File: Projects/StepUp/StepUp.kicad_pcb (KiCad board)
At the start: 2 copper layers, 80 parts, among them J1 Conn_01x02, J4 Conn_01x02, J5 Conn_01x02, J7 Conn_01x02, J8 USB_C_Receptacle_USB2.0_16P, Q1 BSS83P, Q2 BSS83P, SW1 SW_Push, SW2 SW_Push, U1 W25Q128JVS, U2 RP2040, U3 TMC2300-LA, U4 USBLC6-2SC6, U5 MCP73832T-2ACI_OT, U6 NCP1117-3.3_SOT223, U7 MIC2253, U8 COM-09032, Y1 ABM8-272-T3

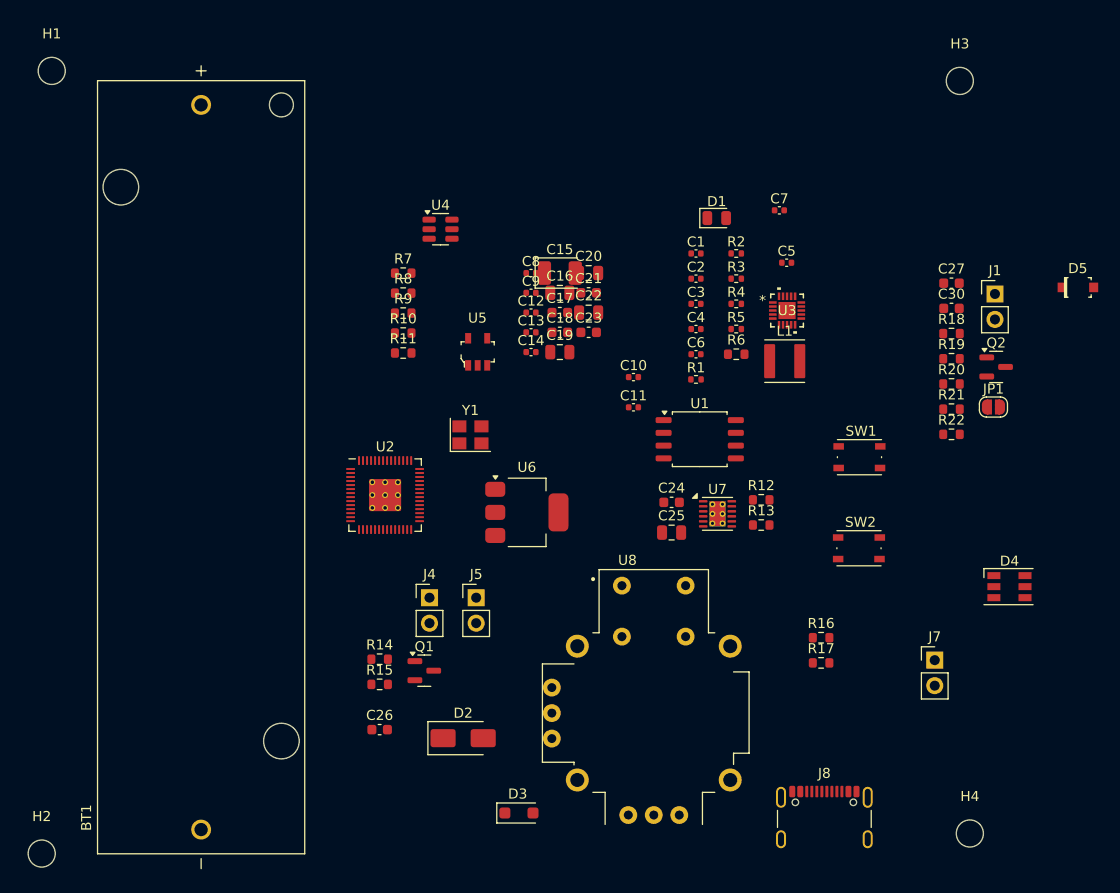
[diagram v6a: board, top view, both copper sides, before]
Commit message: feat(stepup): Schematic + PCB updates
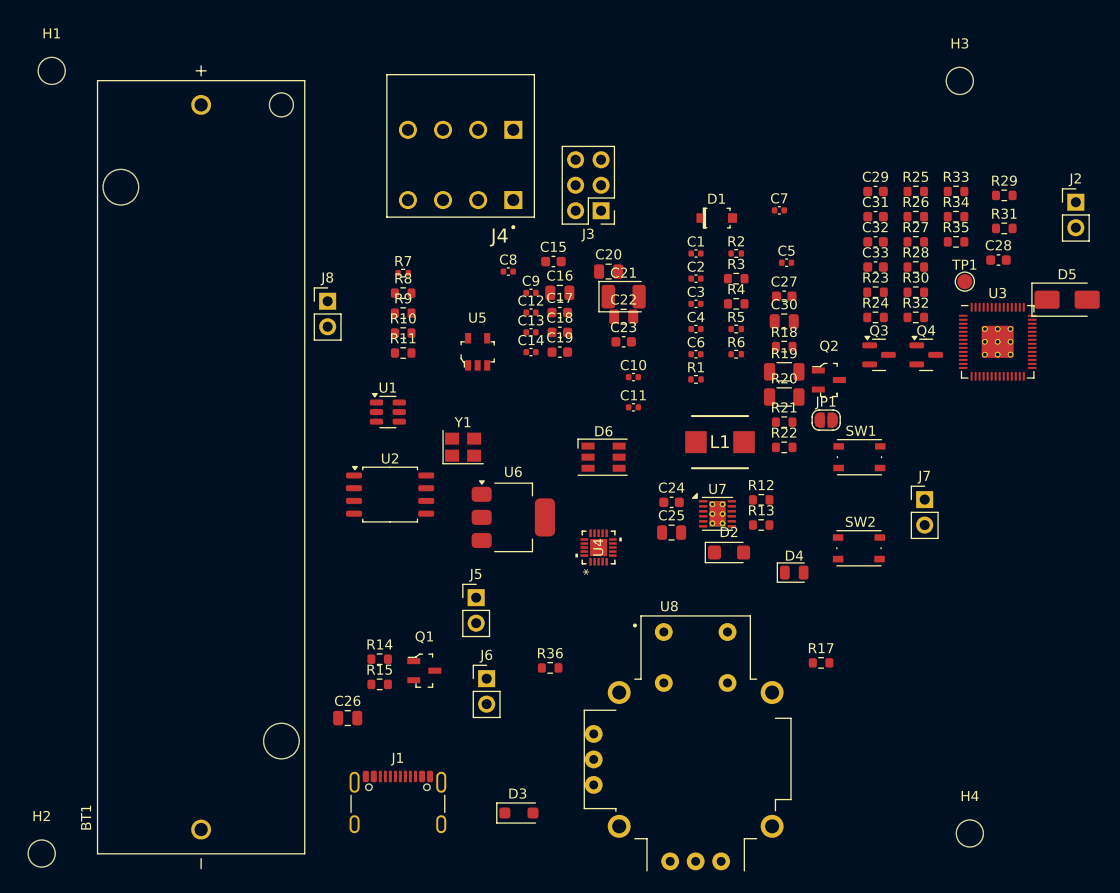
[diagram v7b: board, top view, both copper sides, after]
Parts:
- removed R16: 5.1kR, Resistor_SMD:R_0603_1608Metric
- added C28: 0.01uF, Capacitor_SMD:C_0603_1608Metric, F.Cu at (183.9, 84.4)
- added C29: 100pF, Capacitor_SMD:C_0603_1608Metric, F.Cu at (171.6, 77.5)
- added C31: 0.1uF, Capacitor_SMD:C_0603_1608Metric, F.Cu at (171.6, 80.0)
- added C32: 0.1uF, Capacitor_SMD:C_0603_1608Metric, F.Cu at (171.6, 82.5)
- added C33: 0.1uF, Capacitor_SMD:C_0603_1608Metric, F.Cu at (171.6, 85.1)
- added D6: CLX6F-FKC, LED_SMD:LED_RGB_PLCC-6, F.Cu at (144.5, 104.0)
- added J2: Conn_01x02, Connector_PinHeader_2.54mm:PinHeader_1x02_P2.54mm_Vertical, F.Cu at (191.6, 78.6)
- added J3: Conn_02x03_Counter_Clockwise, Connector_PinHeader_2.54mm:PinHeader_2x03_P2.54mm_Vertical, F.Cu at (144.2, 79.4)
- added J6: Conn_01x02, Connector_PinHeader_2.54mm:PinHeader_1x02_P2.54mm_Vertical, F.Cu at (132.8, 126.1)
- added Q3: BSS83P, Package_TO_SOT_SMD:SOT-23, F.Cu at (171.9, 93.8)
- added Q4: BSS83P, Package_TO_SOT_SMD:SOT-23, F.Cu at (176.6, 93.8)
- added R23: 510R, Resistor_SMD:R_0603_1608Metric, F.Cu at (171.6, 87.6)
- added R24: Rled, Resistor_SMD:R_0603_1608Metric, F.Cu at (171.6, 90.1)
- added R25: 100kR, Resistor_SMD:R_0603_1608Metric, F.Cu at (175.6, 77.5)
- added R26: 620R, Resistor_SMD:R_0603_1608Metric, F.Cu at (175.6, 80.0)
- added R27: 100R, Resistor_SMD:R_0603_1608Metric, F.Cu at (175.6, 82.5)
- added R28: 71.5kR, Resistor_SMD:R_0603_1608Metric, F.Cu at (175.6, 85.1)
- added R29: 10kR, Resistor_SMD:R_0603_1608Metric, F.Cu at (184.4, 77.9)
- added R30: 100kR, Resistor_SMD:R_0603_1608Metric, F.Cu at (175.6, 87.6)
- added R31: 9.09kR, Resistor_SMD:R_0603_1608Metric, F.Cu at (184.4, 81.2)
- added R32: 10kR, Resistor_SMD:R_0603_1608Metric, F.Cu at (175.6, 90.1)
- added R33: 100kR, Resistor_SMD:R_0603_1608Metric, F.Cu at (179.6, 77.5)
- added R34: 100kR, Resistor_SMD:R_0603_1608Metric, F.Cu at (179.6, 80.0)
- added R35: 100kR, Resistor_SMD:R_0603_1608Metric, F.Cu at (179.6, 82.5)
- added R36: 100kR, Resistor_SMD:R_0603_1608Metric, F.Cu at (139.2, 125.0)
- added TP1: TestPoint, TestPoint:TestPoint_Pad_D1.5mm, F.Cu at (180.5, 86.5)
- C15: value 100uF -> 100nF; footprint Capacitor_Tantalum_SMD:CP_EIA-3528-12_Kemet-T -> Capacitor_SMD:C_0603_1608Metric
- C16: value 4.7u -> 10uF
- C17: value 2.2uF -> 100nF
- C18: value 0.01uF -> 100nF
- C19: value 4.7u -> 100nF; footprint Capacitor_SMD:C_0805_2012Metric -> Capacitor_SMD:C_0603_1608Metric
- C20: value 10u -> 10uF
- C21: value 0.1uF -> 100uF; footprint Capacitor_SMD:C_0603_1608Metric -> Capacitor_Tantalum_SMD:CP_EIA-3528-12_Kemet-T
- C22: value 10u -> 4.7u
- C23: value 0.01uF -> 2.2uF
- C24: value 100pF -> 0.01uF
- C25: value 22uF -> 4.7u
- C26: value 0.1uF -> 10uF; footprint Capacitor_SMD:C_0603_1608Metric -> Capacitor_SMD:C_0805_2012Metric
- C30: value 0.1uF -> 22uF; footprint Capacitor_SMD:C_0603_1608Metric -> Capacitor_SMD:C_0805_2012Metric
- D1: value LED -> 1N4148W-TP; footprint LED_SMD:LED_0805_2012Metric -> digikey-footprints:SOD-123
- D2: value SK54A-LTP -> SMF12A; footprint Diode_SMD:D_SMA -> Diode_SMD:D_SMF
- D4: value CLX6F-FKC -> LED; footprint LED_SMD:LED_RGB_PLCC-6 -> LED_SMD:LED_0805_2012Metric
- D5: value 1N4148W-TP -> SK54A-LTP; footprint digikey-footprints:SOD-123 -> Diode_SMD:D_SMA
- J1: value Conn_01x02 -> USB_C_Receptacle_USB2.0_16P; footprint Connector_PinHeader_2.54mm:PinHeader_1x02_P2.54mm_Vertical -> Connector_USB:USB_C_Receptacle_GCT_USB4105-xx-A_16P_TopMnt_Horizontal
- J4: value Conn_01x02 -> TBLH10-350-04BK; footprint Connector_PinHeader_2.54mm:PinHeader_1x02_P2.54mm_Vertical -> Snapeda:CUI_TBLH10-350-04BK
- J8: value USB_C_Receptacle_USB2.0_16P -> Conn_01x02; footprint Connector_USB:USB_C_Receptacle_GCT_USB4105-xx-A_16P_TopMnt_Horizontal -> Connector_PinHeader_2.54mm:PinHeader_1x02_P2.54mm_Vertical
- L1: value 2.2 uH -> ASPI-0530HI-2R2M-T2; footprint Inductor_SMD:L_Abracon_ASPI-4030S -> Samacsys:INDPM5652X300N
- Q1: value BSS83P -> BSS84; footprint Package_TO_SOT_SMD:SOT-23 -> digikey-footprints:SOT-23-3
- Q2: value BSS83P -> 2N7002; footprint Package_TO_SOT_SMD:SOT-23 -> digikey-footprints:SOT-23-3
- R10: value 71.5kR -> 10kR
- R12: value 9.09kR -> 10kR
- R14: value 100R -> 10kR
- R15, R8: value 100kR -> 10kR
- R17: value 5.1kR -> 1kR
- R18: value 10kR -> 100kR
- R19, R20: value 100kR -> 150mR; footprint Resistor_SMD:R_0603_1608Metric -> Resistor_SMD:R_1206_3216Metric
- R22: value 100kR -> 100R
- R3: value 1k -> 5.1kR; footprint Resistor_SMD:R_0402_1005Metric -> Resistor_SMD:R_0603_1608Metric
- R4: value 27 -> 5.1kR; footprint Resistor_SMD:R_0402_1005Metric -> Resistor_SMD:R_0603_1608Metric
- R5: value 27 -> 1k
- R6: value RProg -> 27; footprint Resistor_SMD:R_0603_1608Metric -> Resistor_SMD:R_0402_1005Metric
- R7: value Rled -> 27; footprint Resistor_SMD:R_0603_1608Metric -> Resistor_SMD:R_0402_1005Metric
- R9: value 620R -> 10kR
- U1: value W25Q128JVS -> USBLC6-2SC6; footprint Package_SO:SOIC-8_5.23x5.23mm_P1.27mm -> Package_TO_SOT_SMD:SOT-23-6
- U2: value RP2040 -> W25Q128JVS; footprint RP2040_minimal_r2:RP2040-QFN-56 -> Package_SO:SOIC-8_5.23x5.23mm_P1.27mm
- U3: value TMC2300-LA -> RP2040; footprint Ultra_librarian_footprints:QFN20_3x3_TRI -> RP2040_minimal_r2:RP2040-QFN-56
- U4: value USBLC6-2SC6 -> TMC2300-LA; footprint Package_TO_SOT_SMD:SOT-23-6 -> Ultra_librarian_footprints:QFN20_3x3_TRI
- moved J1 78.9 mm to (124.0, 139.5)
- moved J8 72.2 mm to (117.0, 88.5)
- moved J4 40.5 mm to (135.5, 78.4), turned to 180 degrees
- moved U4 35.4 mm to (144.0, 113.0), turned to 90 degrees
- moved D2 32.3 mm to (157.0, 113.5)
- moved U1 31.2 mm to (123.0, 99.5)
- moved D4 21.5 mm to (163.5, 115.5)
- moved U3 21.2 mm to (183.8, 92.5)
- moved Q2 16.7 mm to (166.9, 96.3)
- moved R21 16.7 mm to (162.5, 100.5)
- moved C27 16.7 mm to (162.5, 88.0)
- moved C30 16.7 mm to (162.5, 90.5)
- moved JP1 16.7 mm to (166.7, 100.3)
- moved R18 16.7 mm to (162.5, 93.0)
- moved R19 16.7 mm to (162.5, 95.5)
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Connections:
- C15 pad 1: /Power/BOOST_VIN -> VMotor
- C15 pad 2: GND -> Net-(U4-VCP)
- C16 pad 1: GND -> VMotor
- C16 pad 2: V_USB -> GND
- C17 pad 1: /Power/BOOST_VIN -> VMotor
- C18 pad 1: /Power/BOOST_VIN -> /Motor Driver/VCC_IO
- C19 pad 1: Net-(J4-Pin_2) -> Net-(U4-1.8VOUT)
- C21 pad 1: Net-(U7-SS) -> /Power/BOOST_VIN
- C22 pad 1: +3V3 -> GND
- C22 pad 2: GND -> V_USB
- C23 pad 1: Net-(C23-Pad1) -> /Power/BOOST_VIN
- C24 pad 1: /Power/BOOST_VOUT -> /Power/BOOST_VIN
- C24 pad 2: Net-(U7-FB) -> GND
- C25 pad 1: /Power/BOOST_VOUT -> Net-(J7-Pin_2)
- C27 pad 1: GND -> Net-(U7-SS)
- C27 pad 2: Vbat_monitor -> GND
- C30 pad 1: GND -> /Power/BOOST_VOUT
- C30 pad 2: VUSB_monitor -> GND
- D2 pad 1: /Power/BOOST_VOUT -> VMotor
- D2 pad 2: Net-(D2-A) -> GND
- D4 pad 1: unconnected-(D4-KB-Pad1) -> Net-(D4-K)
- D4 pad 2: unconnected-(D4-KG-Pad2) -> V_USB
- J5 pad 2: Net-(J5-Pin_2) -> Net-(D3-A)
- J7 pad 2: /Power/BOOST_VIN -> Net-(J7-Pin_2)
- L1 pad 2: Net-(D2-A) -> Net-(D5-A)
- Q1 pad 2: /Power/BOOST_ENABLE -> +3V3
- Q1 pad 3: /Power/MCU_BOOST_EN -> /Motor Driver/VCC_IO
- Q2 pad 1: Net-(D3-A) -> ~{TMC_STBDY}
- Q2 pad 2: Net-(D3-K) -> GND
- Q2 pad 3: Vbat -> Net-(Q1-G)
- R10 pad 1: Net-(U7-OVP) -> /Motor Driver/VCC_IO
- R10 pad 2: /Power/BOOST_VOUT -> GND
- R11 pad 1: GND -> TMC_EN
- R11 pad 2: Net-(U7-OVP) -> GND
- R12 pad 1: Net-(U7-FB) -> TMC_STEP
- R12 pad 2: /Power/BOOST_VOUT -> GND
- R13 pad 1: GND -> TMC_DIR
- R13 pad 2: Net-(U7-FB) -> GND
- R14 pad 1: V_USB -> /Motor Driver/VCC_IO
- R14 pad 2: Net-(Q1-G) -> /Motor Driver/TMC_MS2/AD1
- R15 pad 1: GND -> /Motor Driver/VCC_IO
- R15 pad 2: Net-(Q1-G) -> /Motor Driver/TMC_MS1/AD0
- R17 pad 1: GND -> TMC_UART_RX
- R17 pad 2: Net-(J8-CC2) -> TMC_UART_TX
- R18 pad 1: Net-(D3-A) -> TMC_UART_RX
- R19 pad 2: Vbat_monitor -> Net-(U4-BRA)
- R20 pad 1: Vbat_monitor -> GND
- R20 pad 2: Vbat -> Net-(U4-BRB)
- R21 pad 1: VUSB_monitor -> GND
- R21 pad 2: V_USB -> Net-(D3-A)
- R22 pad 1: GND -> Net-(D3-A)
- R22 pad 2: VUSB_monitor -> Net-(Q3-G)
- R3 pad 1: /MCU/XOUT -> GND
- R3 pad 2: Net-(C2-Pad1) -> Net-(J1-CC1)
- R4 pad 1: /MCU/USB_D+ -> GND
- R4 pad 2: Net-(U2-USB_DP) -> Net-(J1-CC2)
- R5 pad 1: /MCU/USB_D- -> /MCU/XOUT
- R5 pad 2: Net-(U2-USB_DM) -> Net-(C2-Pad1)
- R6 pad 1: GND -> /MCU/USB_D+
- R6 pad 2: Net-(U5-PROG) -> Net-(U3-USB_DP)
- R7 pad 1: Net-(U5-STAT) -> /MCU/USB_D-
- R7 pad 2: Net-(D1-K) -> Net-(U3-USB_DM)
- R8 pad 1: GND -> ~{TMC_STBDY}
- R8 pad 2: /Power/BOOST_ENABLE -> GND
- R9 pad 1: Net-(U7-COMP) -> Net-(Q1-G)
- R9 pad 2: Net-(C23-Pad1) -> +3V3
- SW1 pad 2: Net-(D5-PadK) -> /MCU/RUN
- SW2 pad 2: /MCU/RUN -> Net-(D1-PadK)
- U1 pad 1: /MCU/QSPI_SS -> /MCU/USB_D-_IN
- U1 pad 2: /MCU/QSPI_SD1 -> GND
- U1 pad 3: /MCU/QSPI_SD2 -> /MCU/USB_D+_IN
- U1 pad 4: GND -> /MCU/USB_D+
- U1 pad 5: /MCU/QSPI_SD0 -> Net-(J2-Pin_2)
- U1 pad 6: /MCU/QSPI_SCLK -> /MCU/USB_D-
- U2 pad 1: +3V3 -> /MCU/QSPI_SS
- U2 pad 2: /MCU/GPIO0 -> /MCU/QSPI_SD1
- U2 pad 3: /MCU/GPIO1 -> /MCU/QSPI_SD2
- U2 pad 4: /MCU/GPIO2 -> GND
- U2 pad 5: /MCU/GPIO3 -> /MCU/QSPI_SD0
- U2 pad 6: /MCU/GPIO4 -> /MCU/QSPI_SCLK
- U2 pad 7: /MCU/GPIO5 -> /MCU/QSPI_SD3
- U2 pad 8: /MCU/GPIO6 -> +3V3
- U3 pad 1: unconnected-(U3-OA2-Pad1) -> +3V3
- U3 pad 10: unconnected-(U3-PDN_UART-Pad10) -> +3V3
- U3 pad 11: unconnected-(U3-VIO/NSTDBY-Pad11) -> /MCU/GPIO8
- U3 pad 12: unconnected-(U3-DIAG-Pad12) -> /MCU/GPIO9
- U3 pad 13: unconnected-(U3-1.8VOUT-Pad13) -> /MCU/GPIO10
- U3 pad 14: unconnected-(U3-GND-Pad14) -> /MCU/GPIO11
- U3 pad 15: unconnected-(U3-OB2-Pad15) -> /MCU/GPIO12
- U3 pad 16: unconnected-(U3-BRB-Pad16) -> /MCU/GPIO13
- U3 pad 17: unconnected-(U3-OB1-Pad17) -> TMC_EN
- U3 pad 18: unconnected-(U3-VS-Pad18) -> ~{TMC_STBDY}
- U3 pad 19: unconnected-(U3-OA1-Pad19) -> GND
- U3 pad 2: unconnected-(U3-VCP-Pad2) -> /MCU/UART_0_TX
- U3 pad 20: unconnected-(U3-BRA-Pad20) -> /MCU/XIN
- U3 pad 21: unconnected-(U3-EPAD-Pad21) -> /MCU/XOUT
- U3 pad 3: unconnected-(U3-DIR-Pad3) -> /MCU/UART_0_RX
- U3 pad 4: unconnected-(U3-STEP-Pad4) -> /MCU/GPIO2
- U3 pad 5: unconnected-(U3-MS1_AD0-Pad5) -> /MCU/GPIO3
- U3 pad 6: unconnected-(U3-MS2_AD1-Pad6) -> TMC_UART_TX
- U3 pad 7: unconnected-(U3-EN-Pad7) -> TMC_UART_RX
- U3 pad 8: unconnected-(U3-STEPPER-Pad8) -> /MCU/GPIO6
- U3 pad 9: unconnected-(U3-MODE-Pad9) -> /MCU/GPIO7
- U4 pad 1: /Power/USB_D+_IN -> /Motor Driver/OA2
- U4 pad 2: GND -> Net-(U4-VCP)
- U4 pad 3: /Power/USB_D-_IN -> TMC_DIR
- U4 pad 4: /Power/USB_D- -> TMC_STEP
- U4 pad 5: Net-(J5-Pin_2) -> /Motor Driver/TMC_MS1/AD0
- U4 pad 6: /Power/USB_D+ -> /Motor Driver/TMC_MS2/AD1
- U5 pad 3: Net-(J4-Pin_2) -> Net-(J7-Pin_2)
- U7 pad 7: Net-(D2-A) -> Net-(D5-A)
- U7 pad 8: Net-(D2-A) -> Net-(D5-A)
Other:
- copper layers 2 -> 4

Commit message: feat(schematic): Ready for layout
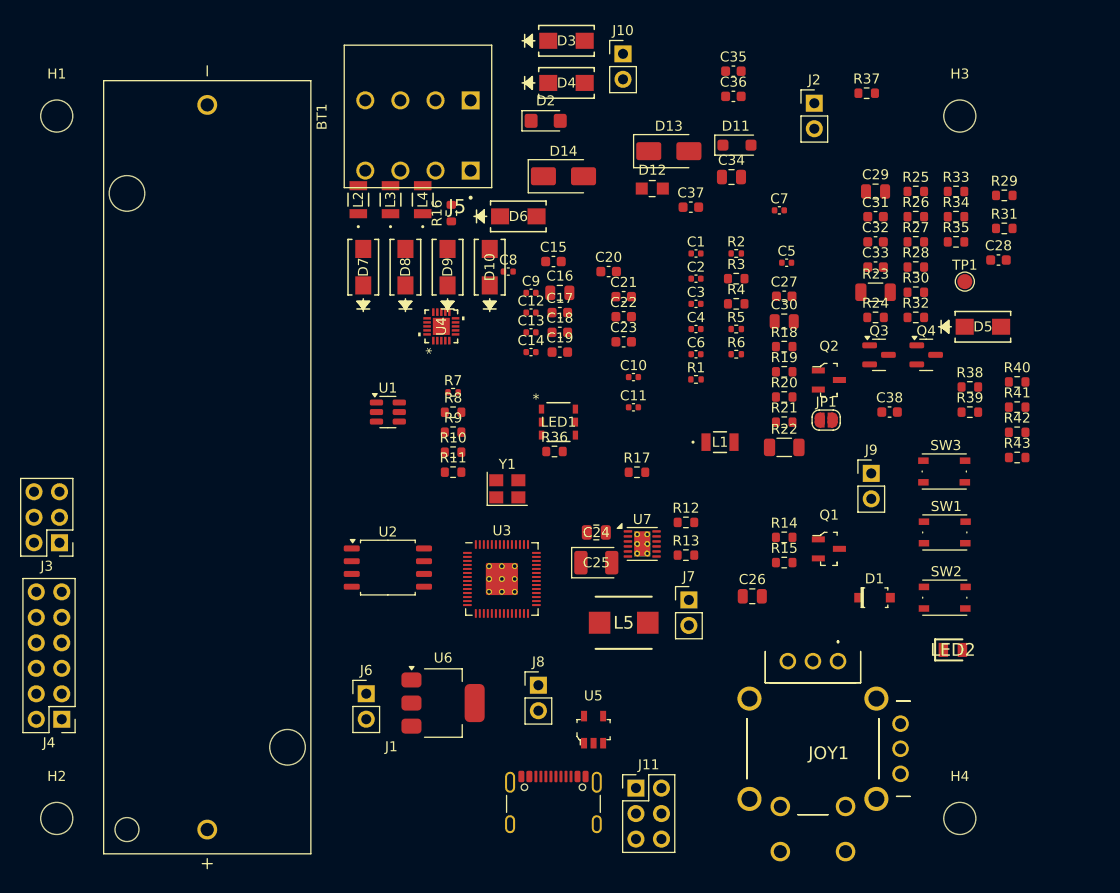
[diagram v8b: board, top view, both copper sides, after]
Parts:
- removed U8: COM-09032, joystick_footprints:XDCR_COM-09032
- added C34: 22uF, Capacitor_SMD:C_0805_2012Metric, F.Cu at (157.2, 76.1)
- added C35: 0.1uF, Capacitor_SMD:C_0603_1608Metric, F.Cu at (157.4, 65.5)
- added C36: 0.1uF, Capacitor_SMD:C_0603_1608Metric, F.Cu at (157.4, 68.0)
- added C37: 0.1uF, Capacitor_SMD:C_0603_1608Metric, F.Cu at (153.2, 79.1)
- added C38: 0.1uF, Capacitor_SMD:C_0603_1608Metric, F.Cu at (173.0, 99.5)
- added D10: SSA33L-E3/61T, Snapeda:DIODE_DO214AC, F.Cu at (133.2, 85.1)
- added D11: PMEG2020EH, Diode_SMD:D_SOD-123F, F.Cu at (157.8, 72.9)
- added D12: LTST-C170KFKT, digikey-footprints:0805, F.Cu at (149.4, 77.2)
- added D13: SK54A-LTP, Diode_SMD:D_SMA, F.Cu at (151.0, 73.5)
- added D14: SK54A-LTP, Diode_SMD:D_SMA, F.Cu at (140.5, 76.0)
- added D7: SSA33L-E3/61T, Snapeda:DIODE_DO214AC, F.Cu at (120.5, 85.1)
- added D8: SSA33L-E3/61T, Snapeda:DIODE_DO214AC, F.Cu at (124.8, 85.1)
- added D9: SSA33L-E3/61T, Snapeda:DIODE_DO214AC, F.Cu at (129.0, 85.1)
- added J10: Conn_01x02, Connector_PinHeader_2.54mm:PinHeader_1x02_P2.54mm_Vertical, F.Cu at (146.4, 63.8)
- added J11: Conn_02x03_Counter_Clockwise, Connector_PinHeader_2.54mm:PinHeader_2x03_P2.54mm_Vertical, F.Cu at (147.7, 137.0)
- added J9: Conn_01x02, Connector_PinHeader_2.54mm:PinHeader_1x02_P2.54mm_Vertical, F.Cu at (171.2, 105.6)
- added JOY1: THB001P, Samacsys:THB001P, F.Cu at (167.9, 124.3)
- added L2: HI1206T500R-10, Snapeda:IND_HI1206T500R-10_LRD, F.Cu at (120.1, 78.3)
- added L3: HI1206T500R-10, Snapeda:IND_HI1206T500R-10_LRD, F.Cu at (123.3, 78.3)
- added L4: HI1206T500R-10, Snapeda:IND_HI1206T500R-10_LRD, F.Cu at (126.5, 78.3)
- added L5: ASPI-0530HI-2R2M-T2, Samacsys:INDPM5652X300N, F.Cu at (146.5, 120.5)
- added LED1: APF3236LSEEZGKQBKC, Snapeda:APF3236LSEEZGKQBKC_KNB, F.Cu at (140.0, 100.5)
- added LED2: LTST-C171GKT, Samacsys:LEDC2012X90N, F.Cu at (179.3, 123.2)
- added R16: 10kR, Resistor_SMD:R_0603_1608Metric, F.Cu at (129.3, 79.7)
- added R37: 100kR, Resistor_SMD:R_0603_1608Metric, F.Cu at (170.7, 67.7)
- added R38: 100kR, Resistor_SMD:R_0603_1608Metric, F.Cu at (181.0, 97.0)
- added R39: 10kR, Resistor_SMD:R_0603_1608Metric, F.Cu at (181.0, 99.5)
- added R40: 10kR, Resistor_SMD:R_0603_1608Metric, F.Cu at (185.7, 96.5)
- added R41: 100kR, Resistor_SMD:R_0603_1608Metric, F.Cu at (185.7, 99.0)
- added R42: 100kR, Resistor_SMD:R_0603_1608Metric, F.Cu at (185.7, 101.5)
- added R43: 620R, Resistor_SMD:R_0603_1608Metric, F.Cu at (185.7, 104.0)
- added SW3: SW_Push, Button_Switch_SMD:SW_Push_1P1T_NO_Vertical_Wuerth_434133025816, F.Cu at (178.4, 105.4)
- C20: value 10uF -> 470pF; footprint Capacitor_SMD:C_0805_2012Metric -> Capacitor_SMD:C_0603_1608Metric
- C21: value 100uF -> 470pF; footprint Capacitor_Tantalum_SMD:CP_EIA-3528-12_Kemet-T -> Capacitor_SMD:C_0603_1608Metric
- C22: value 4.7u -> 470pF; footprint Capacitor_SMD:C_0805_2012Metric -> Capacitor_SMD:C_0603_1608Metric
- C23: value 2.2uF -> 470pF
- C24: value 0.01uF -> 10uF; footprint Capacitor_SMD:C_0603_1608Metric -> Capacitor_SMD:C_0805_2012Metric
- C25: value 4.7u -> 100uF; footprint Capacitor_SMD:C_0805_2012Metric -> Capacitor_Tantalum_SMD:CP_EIA-3528-12_Kemet-T
- C26: value 10uF -> 4.7u
- C27: value 0.1uF -> 2.2uF
- C29: value 100pF -> 4.7u; footprint Capacitor_SMD:C_0603_1608Metric -> Capacitor_SMD:C_0805_2012Metric
- C30: value 22uF -> 10uF
- C32: value 0.1uF -> 0.01uF
- C33: value 0.1uF -> 100pF
- D3: value PMEG2020EH -> SSA33L-E3/61T; footprint Diode_SMD:D_SOD-123F -> Snapeda:DIODE_DO214AC
- D4: value LED -> SSA33L-E3/61T; footprint LED_SMD:LED_0805_2012Metric -> Snapeda:DIODE_DO214AC
- D5: value SK54A-LTP -> SSA33L-E3/61T; footprint Diode_SMD:D_SMA -> Snapeda:DIODE_DO214AC
- D6: value CLX6F-FKC -> SSA33L-E3/61T; footprint LED_SMD:LED_RGB_PLCC-6 -> Snapeda:DIODE_DO214AC
- H1, H2, H3, H4: footprint MountingHole:MountingHole_2.7mm_M2.5 -> MountingHole:MountingHole_3.2mm_M3
- J4: value TBLH10-350-04BK -> Conn_02x06_Counter_Clockwise; footprint Snapeda:CUI_TBLH10-350-04BK -> Connector_PinHeader_2.54mm:PinHeader_2x06_P2.54mm_Vertical
- J5: value Conn_01x02 -> TBLH10-350-04BK; footprint Connector_PinHeader_2.54mm:PinHeader_1x02_P2.54mm_Vertical -> Snapeda:CUI_TBLH10-350-04BK
- L1: value ASPI-0530HI-2R2M-T2 -> HI1206T500R-10; footprint Samacsys:INDPM5652X300N -> Snapeda:IND_HI1206T500R-10_LRD
- R10, R9: value 10kR -> 330R
- R11: value 10kR -> 100R
- R17: value 1kR -> 10kR
- R18, R35: value 100kR -> 10kR
- R19: value 150mR -> 10kR; footprint Resistor_SMD:R_1206_3216Metric -> Resistor_SMD:R_0603_1608Metric
- R20: value 150mR -> 1kR; footprint Resistor_SMD:R_1206_3216Metric -> Resistor_SMD:R_0603_1608Metric
- R22: value 100R -> 150mR; footprint Resistor_SMD:R_0603_1608Metric -> Resistor_SMD:R_1206_3216Metric
- R23: value 510R -> 150mR; footprint Resistor_SMD:R_0603_1608Metric -> Resistor_SMD:R_1206_3216Metric
- R24: value Rled -> 100kR
- R25, R30: value 100kR -> 100R
- R26: value 620R -> 510R
- R27: value 100R -> 620R
- R28: value 71.5kR -> 100kR
- R29: value 10kR -> 620R
- R34: value 100kR -> 71.5kR
- R6, R7: value 27 -> 27R
- R8: value 10kR -> 750R
- moved D3 77.1 mm to (140.8, 62.5)
- moved J4 68.6 mm to (90.5, 130.1)
- moved J3 63.3 mm to (90.3, 112.5)
- moved U3 54.8 mm to (134.4, 116.1)
- moved D4 53.8 mm to (140.8, 66.7)
- moved D2 46.7 mm to (138.7, 70.5)
- moved J8 43.6 mm to (138.0, 126.7)
- moved J5 42.6 mm to (131.2, 75.4), turned to 180 degrees
- moved C26 42.1 mm to (159.3, 117.9)
- moved Q1 42.1 mm to (166.9, 113.1)
- moved R14 42.1 mm to (162.5, 112.0)
- moved R15 42.1 mm to (162.5, 114.5)
- moved D1 41.0 mm to (171.5, 118.0)
- moved U5 39.4 mm to (143.5, 131.2)
- moved J2 27.9 mm to (165.5, 68.7)
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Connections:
- BT1 pad P: Vbat -> Net-(D14-K)
- C20 pad 1: Net-(D3-K) -> GND
- C20 pad 2: GND -> /Motor Driver/OA1_OUT
- C21 pad 1: /Power/BOOST_VIN -> /Motor Driver/OA2_OUT
- C22 pad 2: V_USB -> /Motor Driver/OB1_OUT
- C23 pad 1: /Power/BOOST_VIN -> /Motor Driver/OB2_OUT
- C24 pad 1: /Power/BOOST_VIN -> Net-(D11-K)
- C25 pad 1: Net-(J7-Pin_2) -> /Power/BOOST_VIN
- C26 pad 1: +3V3 -> GND
- C26 pad 2: GND -> V_USB
- C27 pad 1: Net-(U7-SS) -> /Power/BOOST_VIN
- C28 pad 1: Net-(C28-Pad1) -> /Power/BOOST_VIN
- C29 pad 1: /Power/BOOST_VOUT -> Net-(J8-Pin_2)
- C29 pad 2: Net-(U7-FB) -> GND
- C30 pad 1: /Power/BOOST_VOUT -> +3V3
- C31 pad 1: GND -> Net-(U7-SS)
- C31 pad 2: Vbat_monitor -> GND
- C32 pad 1: GND -> Net-(C32-Pad1)
- C32 pad 2: VUSB_monitor -> GND
- C33 pad 1: +3V3 -> /Power/BOOST_VOUT
- C33 pad 2: GND -> Net-(U7-FB)
- D3 pad 1: Net-(D3-K) -> VMotor
- D3 pad 2: Net-(D3-A) -> /Motor Driver/OA1_OUT
- D4 pad 1: Net-(D4-K) -> /Motor Driver/OA1_OUT
- D4 pad 2: V_USB -> GND
- D5 pad 1: /Power/BOOST_VOUT -> VMotor
- D5 pad 2: Net-(D5-A) -> /Motor Driver/OA2_OUT
- D6 pad 1: unconnected-(D6-KB-Pad1) -> /Motor Driver/OA2_OUT
- D6 pad 2: unconnected-(D6-KG-Pad2) -> GND
- J6 pad 1: Vbat -> V_USB
- J6 pad 2: /Power/BOOST_VIN -> Net-(D11-A)
- J7 pad 2: Net-(J7-Pin_2) -> /Power/BOOST_VIN
- J8 pad 1: VMotor -> Vbat
- J8 pad 2: /Power/BOOST_VOUT -> Net-(J8-Pin_2)
- L1 pad 1: /Power/BOOST_VIN -> /Motor Driver/OA1_OUT
- L1 pad 2: Net-(D5-A) -> /Motor Driver/OA1
- Q2 pad 1: ~{TMC_STBDY} -> Net-(Q2-G)
- Q3 pad 2: Net-(D3-K) -> Net-(D11-K)
- R10 pad 1: /Motor Driver/VCC_IO -> /MCU/LED_BLUE
- R10 pad 2: GND -> Net-(LED1-Pad6)
- R11 pad 1: TMC_EN -> ~{TMC_STBDY}
- R11 pad 2: GND -> Net-(Q2-G)
- R12 pad 1: TMC_STEP -> Net-(Q2-G)
- R13 pad 1: TMC_DIR -> Net-(Q1-G)
- R13 pad 2: GND -> +3V3
- R14 pad 1: /Motor Driver/VCC_IO -> TMC_EN
- R14 pad 2: /Motor Driver/TMC_MS2/AD1 -> GND
- R15 pad 1: /Motor Driver/VCC_IO -> TMC_STEP
- R15 pad 2: /Motor Driver/TMC_MS1/AD0 -> GND
- R17 pad 1: TMC_UART_RX -> /Motor Driver/VCC_IO
- R17 pad 2: TMC_UART_TX -> GND
- R18 pad 1: TMC_UART_RX -> /Motor Driver/VCC_IO
- R18 pad 2: GND -> /Motor Driver/TMC_MS2/AD1
- R19 pad 1: GND -> /Motor Driver/VCC_IO
- R19 pad 2: Net-(U4-BRA) -> /Motor Driver/TMC_MS1/AD0
- R20 pad 1: GND -> TMC_UART_RX
- R20 pad 2: Net-(U4-BRB) -> TMC_UART_TX
- R21 pad 1: GND -> TMC_UART_RX
- R21 pad 2: Net-(D3-A) -> GND
- R22 pad 1: Net-(D3-A) -> GND
- R22 pad 2: Net-(Q3-G) -> Net-(U4-BRA)
- R23 pad 2: Net-(U5-PROG) -> Net-(U4-BRB)
- R24 pad 1: Net-(U5-STAT) -> GND
- R24 pad 2: Net-(D4-K) -> Net-(D11-A)
- R25 pad 1: GND -> Net-(D11-A)
- R25 pad 2: /Power/BOOST_ENABLE -> Net-(Q3-G)
- R26 pad 1: Net-(U7-COMP) -> GND
- R26 pad 2: Net-(C28-Pad1) -> Net-(U5-PROG)
- R27 pad 1: V_USB -> Net-(U5-STAT)
- R27 pad 2: Net-(Q4-G) -> Net-(D12-Pad2)
- R28 pad 1: Net-(U7-OVP) -> GND
- R28 pad 2: /Power/BOOST_VOUT -> /Power/BOOST_ENABLE
- R29 pad 1: GND -> Net-(U7-COMP)
- R29 pad 2: Net-(U7-OVP) -> Net-(C32-Pad1)
- R30 pad 1: GND -> V_USB
- R31 pad 1: Net-(U7-FB) -> Net-(U7-OVP)
- R32 pad 2: Net-(U7-FB) -> Net-(U7-OVP)
- R33 pad 1: Vbat_monitor -> GND
- R33 pad 2: Vbat -> Net-(Q4-G)
- R34 pad 1: GND -> Net-(U7-FB)
- R34 pad 2: Vbat_monitor -> /Power/BOOST_VOUT
- R35 pad 1: VUSB_monitor -> GND
- R35 pad 2: V_USB -> Net-(U7-FB)
- R36 pad 1: GND -> Vbat_monitor
- R36 pad 2: VUSB_monitor -> Vbat
- R8 pad 1: ~{TMC_STBDY} -> /MCU/LED_RED
- R8 pad 2: GND -> Net-(LED1-Pad4)
- R9 pad 1: Net-(Q1-G) -> /MCU/LED_GREEN
- R9 pad 2: +3V3 -> Net-(LED1-Pad5)
- U3 pad 27: TMC_DIAG -> /MCU/GPIO16
- U3 pad 31: /MCU/GPIO20 -> TMC_DIAG
- U3 pad 32: /MCU/GPIO21 -> VUSB_monitor
- U3 pad 35: /MCU/GPIO23 -> /MCU/LED_RED
- U3 pad 36: /MCU/GPIO24 -> /MCU/LED_GREEN
- U3 pad 37: VUSB_monitor -> /MCU/LED_BLUE
- U3 pad 4: /MCU/GPIO2 -> TMC_STEP
- U3 pad 41: /MCU/GPIO29_ADC3 -> Vmotor_monitor
- U3 pad 5: /MCU/GPIO3 -> TMC_DIR
- U5 pad 3: Net-(J7-Pin_2) -> Net-(J8-Pin_2)
- U6 pad 3: Net-(D3-K) -> Net-(D11-K)
- U7 pad 7: Net-(D5-A) -> Net-(D13-A)
- U7 pad 8: Net-(D5-A) -> Net-(D13-A)
